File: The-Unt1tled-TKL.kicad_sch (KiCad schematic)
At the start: 211 parts, among them J1 USB_C_Receptacle, J2 AVR-ISP-6, SW1 SW_Reset, SW2 SW_Boot, U1 ATmega324A-P, Y1 20MHz

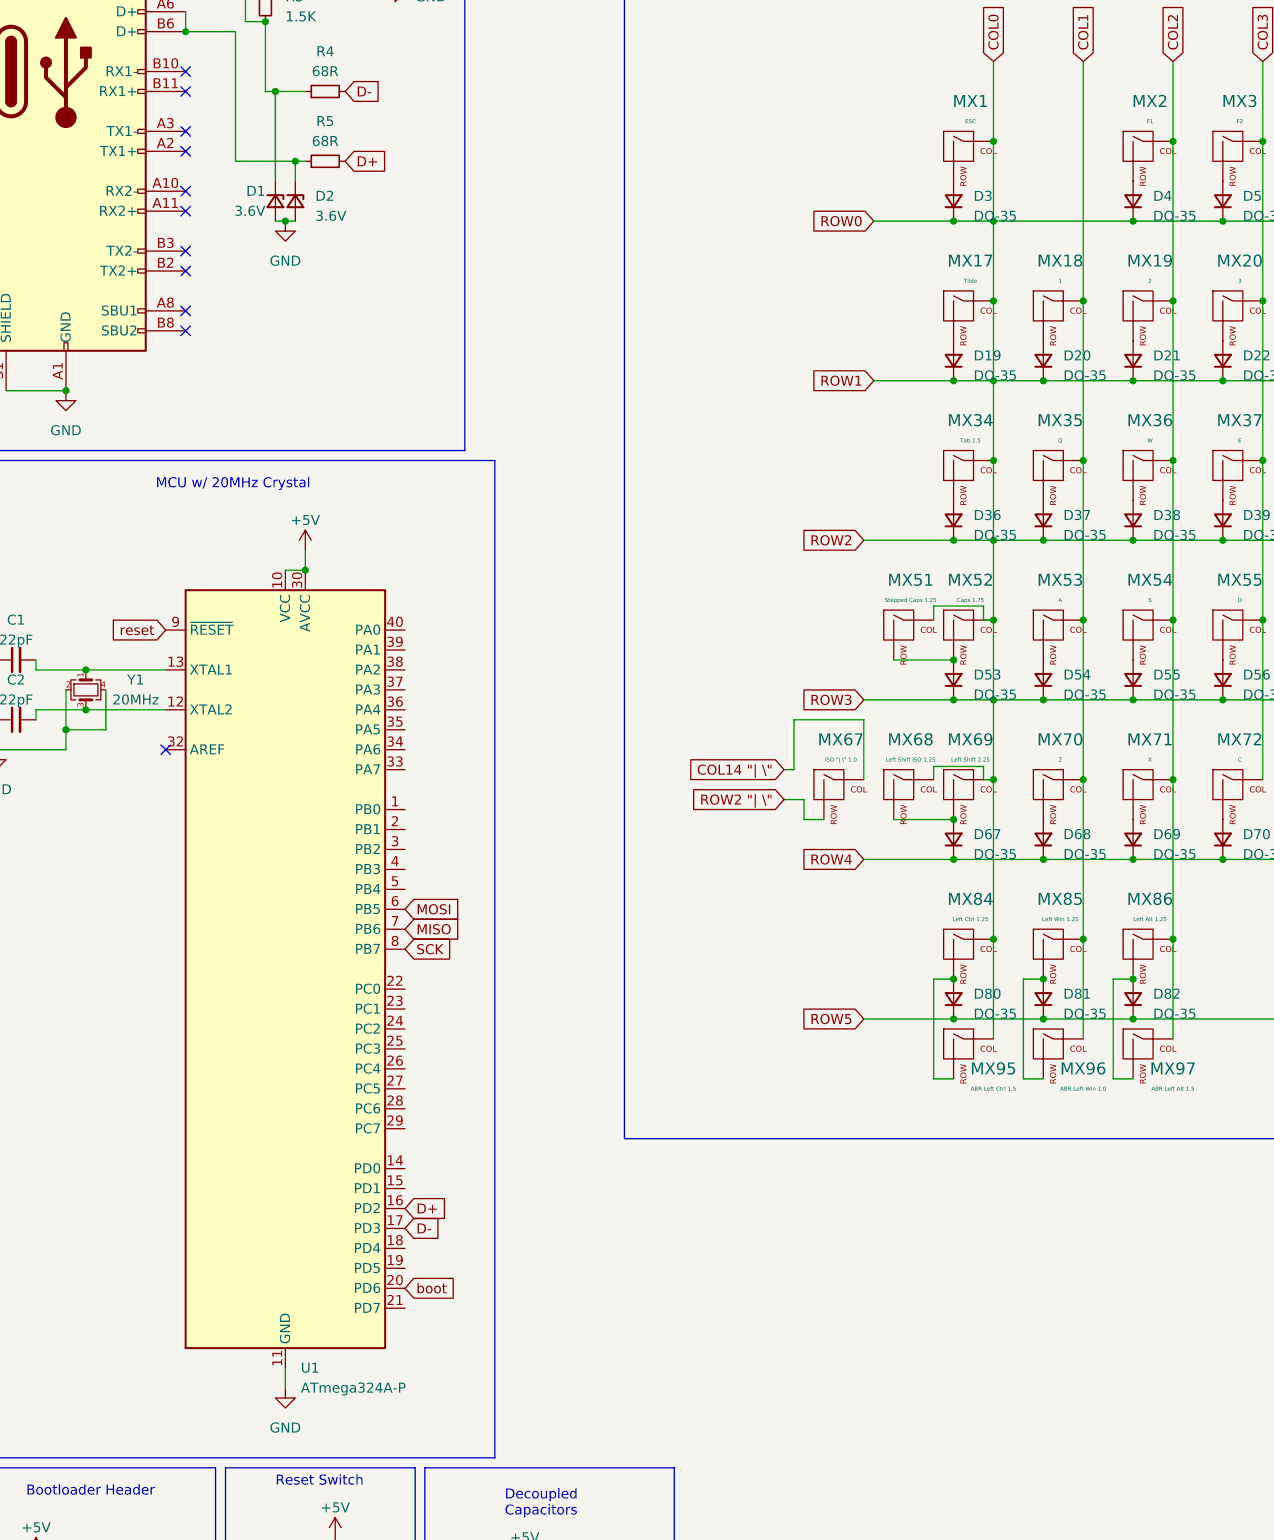
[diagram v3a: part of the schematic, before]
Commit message: Part placement and wireing
Placed diodes. Still need to place other parts in their final position. Started wiring.
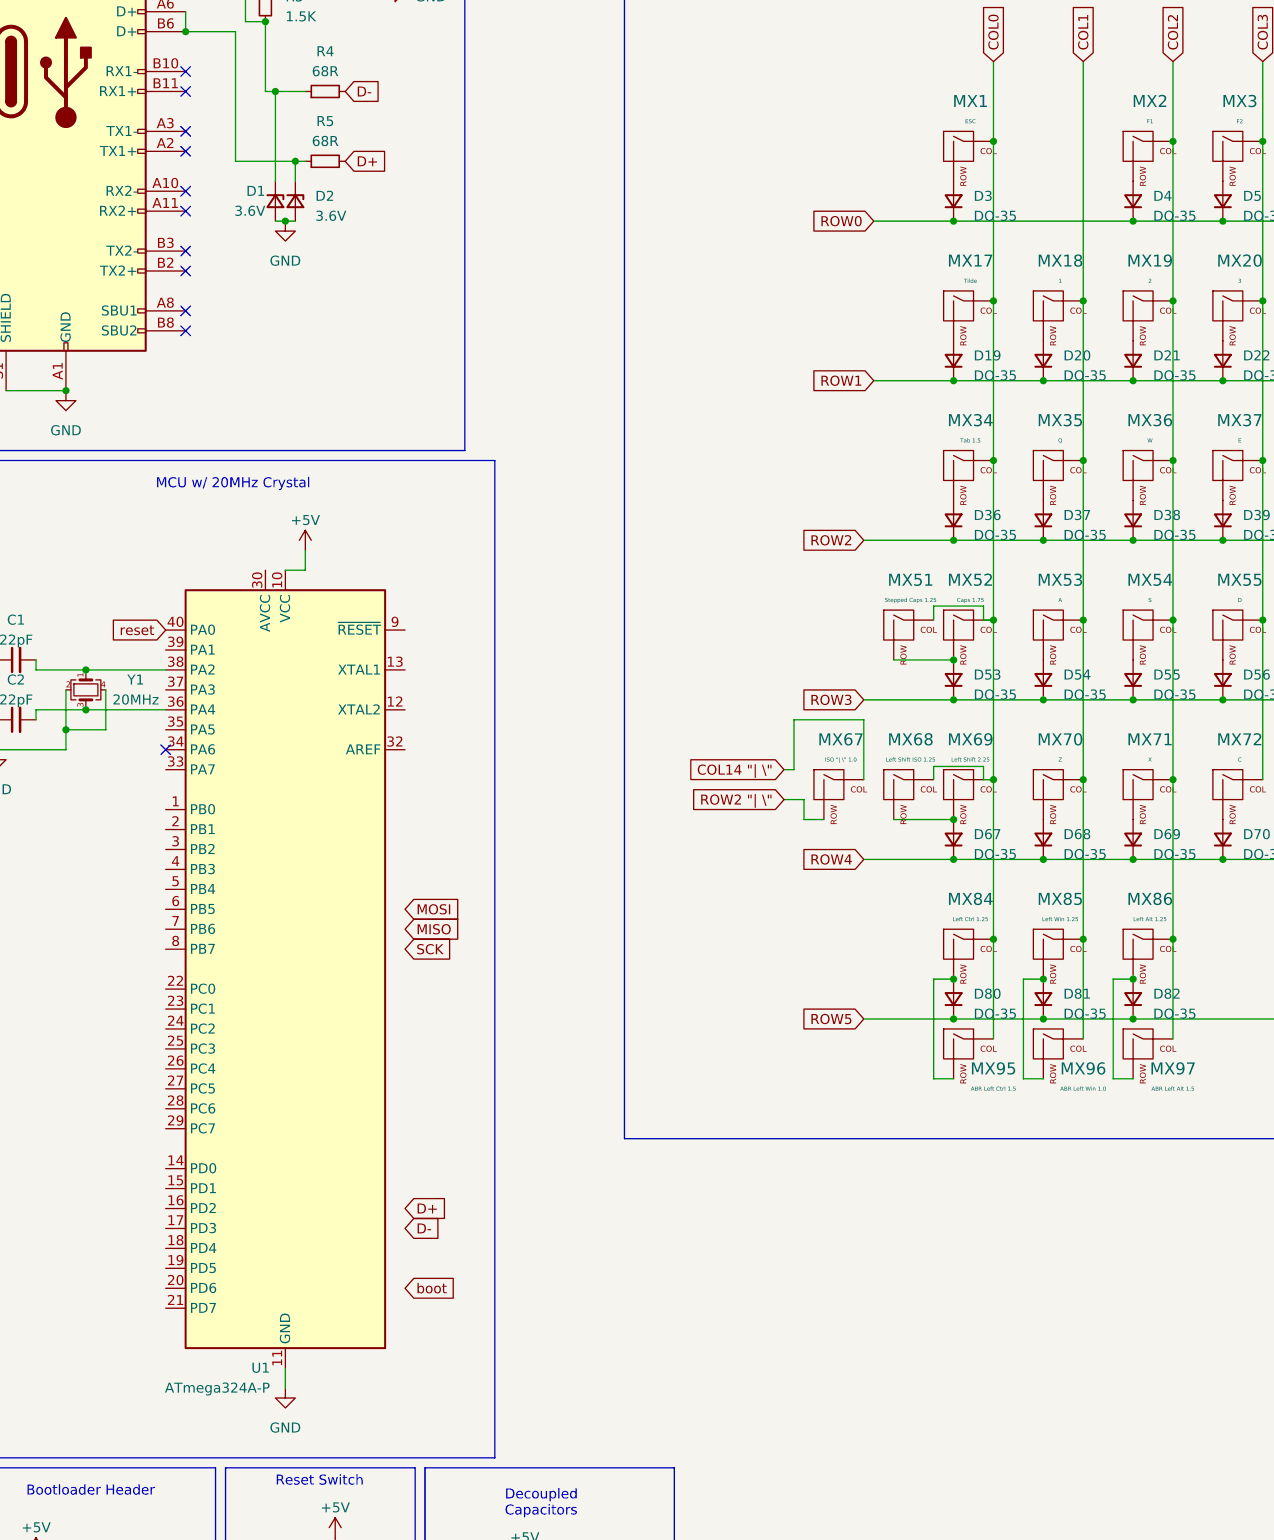
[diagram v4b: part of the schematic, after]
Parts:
- MX30: footprint MX_Only:MXOnly-1U-NoLED -> MX_Only:MXOnly-2U-NoLED
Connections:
- net +5V: no longer U1.30 (AVCC)
- net COL0: no longer D10.1 (K), D11.1 (K), D12.1 (K), D13.1 (K), D14.1 (K), D15.1 (K), D16.1 (K), D17.1 (K), D18.1 (K), D19.1 (K), D20.1 (K), D21.1 (K), D22.1 (K), D23.1 (K), D24.1 (K), D25.1 (K), D26.1 (K), D27.1 (K), D28.1 (K), D29.1 (K), D3.1 (K), D30.1 (K), D31.1 (K), D32.1 (K), D33.1 (K), D34.1 (K), D35.1 (K), D36.1 (K), D37.1 (K), D38.1 (K), D39.1 (K), D4.1 (K), D40.1 (K), D41.1 (K), D42.1 (K), D43.1 (K), D44.1 (K), D45.1 (K), D46.1 (K), D47.1 (K), D48.1 (K), D49.1 (K), D5.1 (K), D50.1 (K), D51.1 (K), D52.1 (K), D53.1 (K), D54.1 (K), D55.1 (K), D56.1 (K), D57.1 (K), D58.1 (K), D59.1 (K), D6.1 (K), D60.1 (K), D61.1 (K), D62.1 (K), D63.1 (K), D64.1 (K), D65.1 (K), D66.1 (K), D7.1 (K), D8.1 (K), D9.1 (K)
- net D+: no longer U1.16 (PD2)
- net D-: no longer U1.17 (PD3)
- net MISO: no longer U1.7 (PB6)
- net MOSI: no longer U1.6 (PB5)
- net SCK: no longer U1.8 (PB7)
- net boot: no longer U1.20 (PD6)
- net reset: now also U1.40 (PA0); no longer U1.9 (~{RESET})
- net at C2.2, Y1.3: now also U1.36 (PA4); no longer U1.12 (XTAL2)
- net at C1.2, Y1.1: now also U1.38 (PA2); no longer U1.13 (XTAL1)
- new net ROW0: D10.1 (K), D11.1 (K), D12.1 (K), D13.1 (K), D14.1 (K), D15.1 (K), D16.1 (K), D17.1 (K), D18.1 (K), D3.1 (K), D4.1 (K), D5.1 (K), D6.1 (K), D7.1 (K), D8.1 (K), D9.1 (K)
- new net ROW1: D19.1 (K), D20.1 (K), D21.1 (K), D22.1 (K), D23.1 (K), D24.1 (K), D25.1 (K), D26.1 (K), D27.1 (K), D28.1 (K), D29.1 (K), D30.1 (K), D31.1 (K), D32.1 (K), D33.1 (K), D34.1 (K), D35.1 (K)
- new net ROW2: D36.1 (K), D37.1 (K), D38.1 (K), D39.1 (K), D40.1 (K), D41.1 (K), D42.1 (K), D43.1 (K), D44.1 (K), D45.1 (K), D46.1 (K), D47.1 (K), D48.1 (K), D49.1 (K), D50.1 (K), D51.1 (K), D52.1 (K)
- new net ROW3: D53.1 (K), D54.1 (K), D55.1 (K), D56.1 (K), D57.1 (K), D58.1 (K), D59.1 (K), D60.1 (K), D61.1 (K), D62.1 (K), D63.1 (K), D64.1 (K), D65.1 (K), D66.1 (K)
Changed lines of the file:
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@@
   (junction (at 173.99 133.35) (diameter 0) (color 0 0 0 0)
   )
-  (junction (at 144.78 113.03) (diameter 0) (color 0 0 0 0)
-  )
   (junction (at 213.36 62.23) (diameter 0) (color 0 0 0 0)
   )
@@
   (junction (at 139.7 113.03) (diameter 0) (color 0 0 0 0)
   )
-  (junction (at 144.78 72.39) (diameter 0) (color 0 0 0 0)
-  )
   (junction (at 276.86 72.39) (diameter 0) (color 0 0 0 0)
   )
@@
   (junction (at 231.14 113.03) (diameter 0) (color 0 0 0 0)
   )
-  (junction (at 57.15 116.84) (diameter 0) (color 0 0 0 0)
-  )
   (junction (at 321.31 102.87) (diameter 0) (color 0 0 0 0)
   )
@@
   (junction (at 242.57 92.71) (diameter 0) (color 0 0 0 0)
   )
-  (junction (at 144.78 133.35) (diameter 0) (color 0 0 0 0)
-  )
   (junction (at 247.65 123.19) (diameter 0) (color 0 0 0 0)
   )
@@
   (junction (at 151.13 133.35) (diameter 0) (color 0 0 0 0)
   )
-  (junction (at 144.78 92.71) (diameter 0) (color 0 0 0 0)
-  )
   (junction (at 288.29 173.99) (diameter 0) (color 0 0 0 0)
   )
@@
     (stroke (width 0) (type default))
   )
-  (wire (pts (xy 144.78 133.35) (xy 144.78 143.51))
-    (stroke (width 0) (type default))
-  )
   (wire (pts (xy 308.61 128.27) (xy 316.23 128.27))
     (stroke (width 0) (type default))
@@
     (stroke (width 0) (type default))
   )
-  (wire (pts (xy 144.78 113.03) (xy 151.13 113.03))
-    (stroke (width 0) (type default))
-  )
   (wire (pts (xy 265.43 92.71) (xy 276.86 92.71))
     (stroke (width 0) (type default))
@@
     (stroke (width 0) (type default))
   )
-  (wire (pts (xy 144.78 82.55) (xy 144.78 92.71))
-    (stroke (width 0) (type default))
-  )
   (wire (pts (xy 231.14 153.67) (xy 242.57 153.67))
     (stroke (width 0) (type default))
@@
     (stroke (width 0) (type default))
   )
-  (wire (pts (xy 144.78 62.23) (xy 144.78 72.39))
+  (wire (pts (xy 144.78 62.23) (xy 144.78 82.55))
     (stroke (width 0) (type default))
   )
@@
     (stroke (width 0) (type default))
   )
-  (wire (pts (xy 144.78 102.87) (xy 144.78 113.03))
+  (wire (pts (xy 144.78 102.87) (xy 144.78 123.19))
     (stroke (width 0) (type default))
   )
@@
     (stroke (width 0) (type default))
   )
-  (wire (pts (xy 144.78 92.71) (xy 144.78 102.87))
+  (wire (pts (xy 144.78 82.55) (xy 144.78 102.87))
     (stroke (width 0) (type default))
   )
@@
     (stroke (width 0) (type default))
   )
-  (wire (pts (xy 144.78 72.39) (xy 162.56 72.39))
+  (wire (pts (xy 139.7 72.39) (xy 162.56 72.39))
     (stroke (width 0) (type default))
   )
@@
     (stroke (width 0) (type default))
   )
-  (wire (pts (xy 144.78 113.03) (xy 144.78 123.19))
-    (stroke (width 0) (type default))
-  )
   (wire (pts (xy 76.2 243.84) (xy 85.09 243.84))
     (stroke (width 0) (type default))
   )
-  (wire (pts (xy 139.7 92.71) (xy 144.78 92.71))
+  (wire (pts (xy 139.7 92.71) (xy 151.13 92.71))
     (stroke (width 0) (type default))
   )
@@
     (stroke (width 0) (type default))
   )
-  (wire (pts (xy 144.78 133.35) (xy 151.13 133.35))
-    (stroke (width 0) (type default))
-  )
   (wire (pts (xy 151.13 153.67) (xy 162.56 153.67))
     (stroke (width 0) (type default))
@@
     (stroke (width 0) (type default))
   )
-  (wire (pts (xy 144.78 113.03) (xy 139.7 113.03))
+  (wire (pts (xy 139.7 113.03) (xy 151.13 113.03))
     (stroke (width 0) (type default))
   )
@@
     (stroke (width 0) (type default))
   )
-  (wire (pts (xy 144.78 123.19) (xy 144.78 133.35))
+  (wire (pts (xy 144.78 123.19) (xy 144.78 143.51))
     (stroke (width 0) (type default))
   )
@@
     (stroke (width 0) (type default))
   )
-  (wire (pts (xy 144.78 133.35) (xy 139.7 133.35))
+  (wire (pts (xy 139.7 133.35) (xy 151.13 133.35))
     (stroke (width 0) (type default))
   )
@@
     (stroke (width 0) (type default))
   )
-  (wire (pts (xy 144.78 72.39) (xy 144.78 82.55))
-    (stroke (width 0) (type default))
-  )
   (wire (pts (xy 128.27 135.89) (xy 119.38 135.89))
     (stroke (width 0) (type default))
@@
     (stroke (width 0) (type default))
   )
-  (wire (pts (xy 144.78 72.39) (xy 139.7 72.39))
-    (stroke (width 0) (type default))
-  )
   (wire (pts (xy 167.64 143.51) (xy 167.64 163.83))
     (stroke (width 0) (type default))
@@
     (stroke (width 0) (type default))
   )
-  (wire (pts (xy 144.78 92.71) (xy 151.13 92.71))
-    (stroke (width 0) (type default))
-  )
   (wire (pts (xy 55.88 64.77) (xy 48.26 64.77))
     (stroke (width 0) (type default))
@@
     )
   )
-  (symbol (lib_id "MCU_Microchip_ATmega:ATmega324A-P") (at 54.61 167.64 0) (unit 1)
-    (in_bom yes) (on_board yes) (dnp no) (fields_autoplaced)
-    (property "Reference" "U1" (at 56.5659 218.44 0)
+  (symbol (lib_id "MCU_Microchip_ATmega:ATmega324A-P") (at 54.61 167.64 0) (mirror y) (unit 1)
+    (in_bom yes) (on_board yes) (dnp no)
+    (property "Reference" "U1" (at 52.6541 218.44 0)
       (effects (font (size 1.27 1.27)) (justify left))
     )
-    (property "Value" "ATmega324A-P" (at 56.5659 220.98 0)
+    (property "Value" "ATmega324A-P" (at 52.6541 220.98 0)
       (effects (font (size 1.27 1.27)) (justify left))
     )
@@
       (effects (font (size 0.508 0.508)))
     )
-    (property "Footprint" "MX_Only:MXOnly-1U-NoLED" (at 301.625 84.455 0)
+    (property "Footprint" "MX_Only:MXOnly-2U-NoLED" (at 301.625 84.455 0)
       (effects (font (size 1.524 1.524)) hide)
     )
